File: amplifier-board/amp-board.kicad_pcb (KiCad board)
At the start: 2 copper layers, 70.1 x 50 mm, 32 parts, among them K1 CONN_3, P1 CONN_7, P2 CONN_7, U1 AD8618, U3 INA128, U4 ad7694

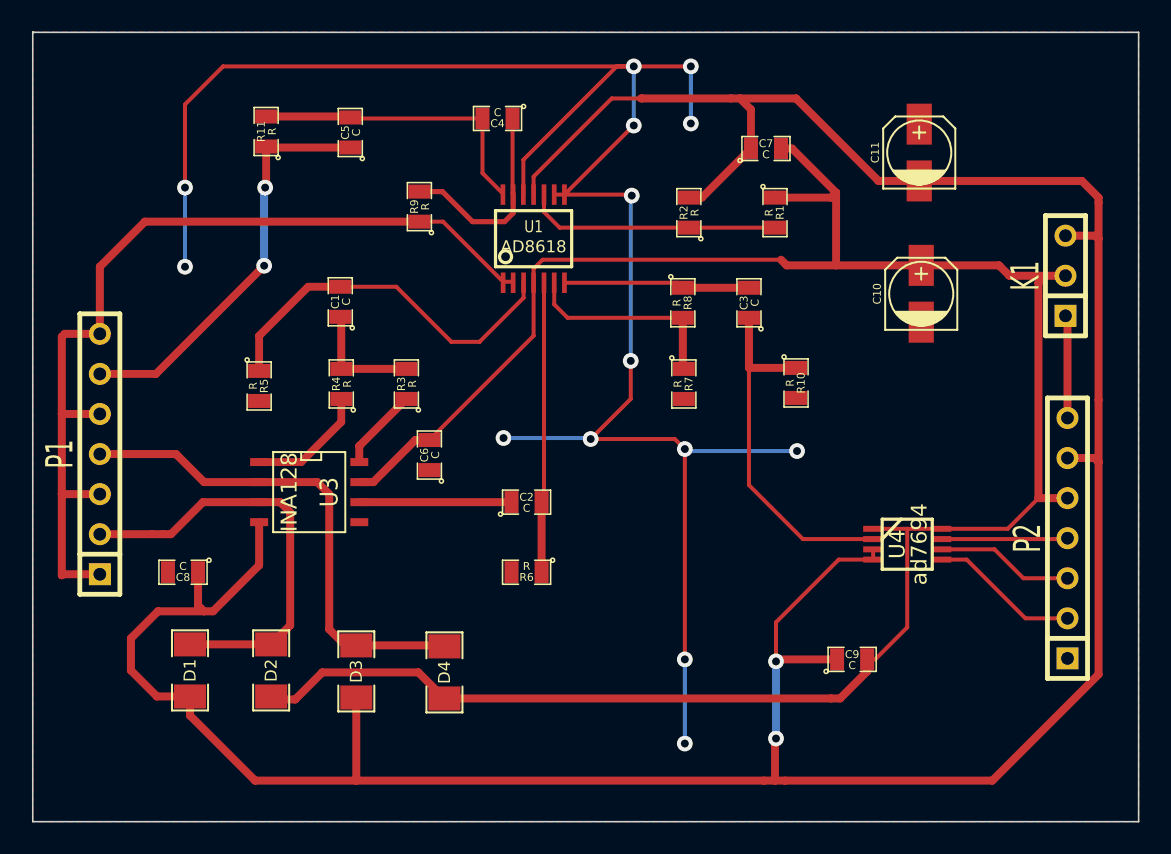
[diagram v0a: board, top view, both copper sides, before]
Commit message: fixed diodes on amplifier pcb
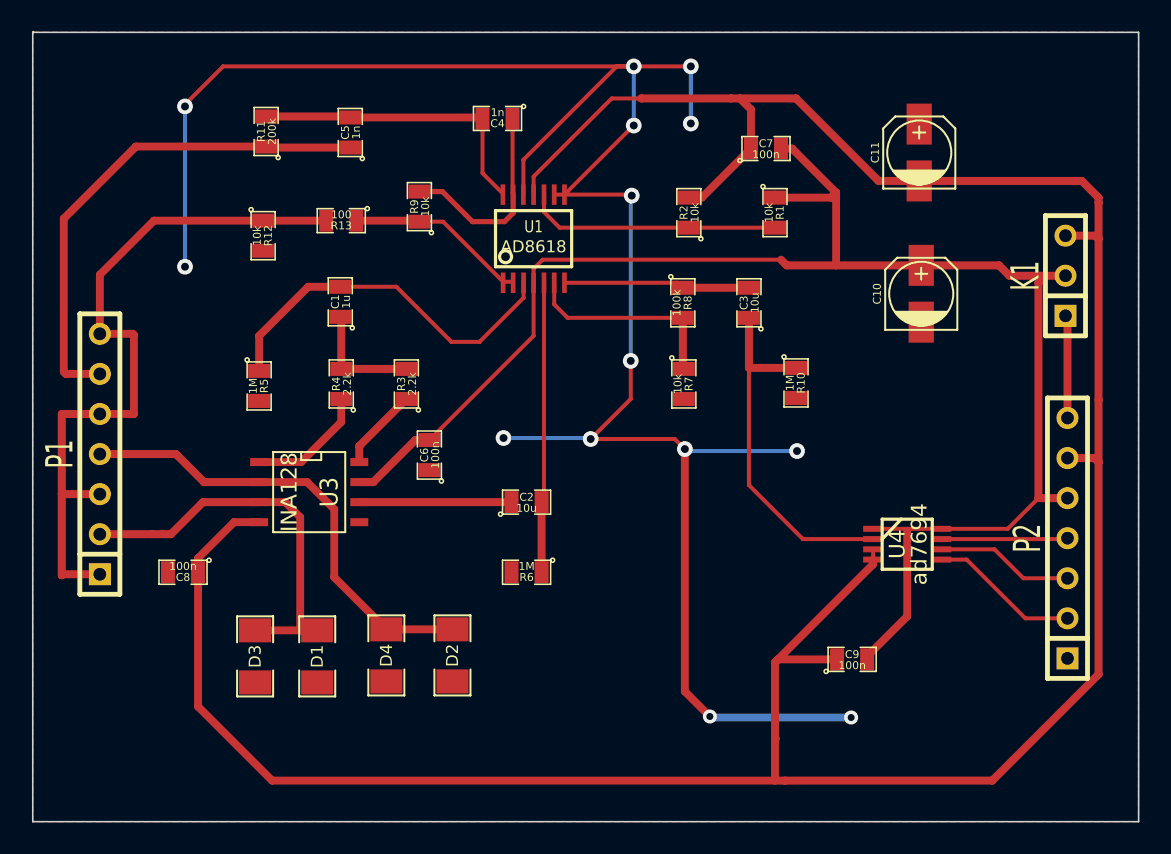
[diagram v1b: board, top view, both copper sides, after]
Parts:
- added R12: 10k, SM0805, F.Cu at (26.7, 25.0)
- added R13: 100, SM0805, F.Cu at (31.6, 24.0)
- C1: value C -> 1u
- C2, C3: value C -> 10u
- C4, C5: value C -> 1n
- C6, C7, C8, C9: value C -> 100n
- R1, R2, R7, R9: value R -> 10k
- R10, R5, R6: value R -> 1M
- R11: value R -> 200k
- R3, R4: value R -> 2.2k
- R8: value R -> 100k
- moved D2 11.5 mm to (38.7, 51.6), turned to 270 degrees
- moved D1 8.11 mm to (30.1, 51.6)
- moved D3 6.48 mm to (26.2, 51.6), turned to 90 degrees
- moved D4 3.84 mm to (34.5, 51.6)
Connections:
- D1 pad 1: N-0000020 -> N-0000018
- D1 pad 2: GND -> AGND
- D2 pad 1: +5V -> N-0000019
- D2 pad 2: N-0000020 -> AGND
- D3 pad 1: N-0000023 -> AGND
- D3 pad 2: GND -> N-0000018
- D4 pad 1: +5V -> AGND
- D4 pad 2: N-0000023 -> N-0000019
- P1 pad 1: N-0000021 (its old number) -> N-0000023
- P1 pad 2: N-0000020 -> N-0000018
- P1 pad 3: N-0000021 (its old number) -> N-0000023
- P1 pad 4: N-0000023 -> N-0000019
- P1 pad 5: N-0000021 (its old number) -> N-0000023
- P1 pad 7: N-0000021 (its old number) -> N-0000023
- R9 pad 1: N-0000021 (its old number) -> N-000002
- U1 pad 1: N-0000021 (its old number) -> N-000002
- U1 pad 2: N-0000021 (its old number) -> N-000002
- U3 pad 2: N-0000023 -> N-0000019
- U3 pad 3: N-0000020 -> N-0000018
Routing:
- net N-0000021 (its old number): track 58.1 -> 0.00 mm
- net +5V: track 145.5 -> 104.3 mm
- net N-0000019: track 0.00 -> 29.5 mm
- net N-0000020: track 27.2 -> 0.00 mm
- net N-0000018: track 0.00 -> 25.0 mm
- net GND: track 197.7 -> 182.1 mm, vias 2 -> 0
- net N-0000023: track 31.8 -> 46.4 mm
- net N-000002: track 0.00 -> 11.5 mm
- net AGND: track 127.8 -> 135.7 mm
- net N-000001: track 26.2 -> 32.1 mm, vias 2 -> 0

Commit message: added discontinued notice
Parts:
- added C12: C, SM0805, F.Cu at (58.4, 29.4)
- moved R10 10.4 mm to (57.3, 44.2), turned to 180 degrees
- moved C3 5.24 mm to (58.5, 34.4)
- moved C9 3.84 mm to (66.3, 48.8)
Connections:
- D1 pad 2: AGND -> +5V
- D2 pad 2: AGND -> +5V
- D3 pad 1: AGND -> GND
- D4 pad 1: AGND -> GND
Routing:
- net +5V: track 104.3 -> 142.7 mm
- net N-000008: track 11.8 -> 21.6 mm
- net AGND: track 135.7 -> 126.4 mm
- net N-000007: track 22.9 -> 16.0 mm
- net N-0000019: track 13.1 -> 18.3 mm
- net GND: track 182.1 -> 187.1 mm, vias 0 -> 2
